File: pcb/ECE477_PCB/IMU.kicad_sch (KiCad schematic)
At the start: 8 parts, among them U5 MPU-9250, U6 LSM6DS3

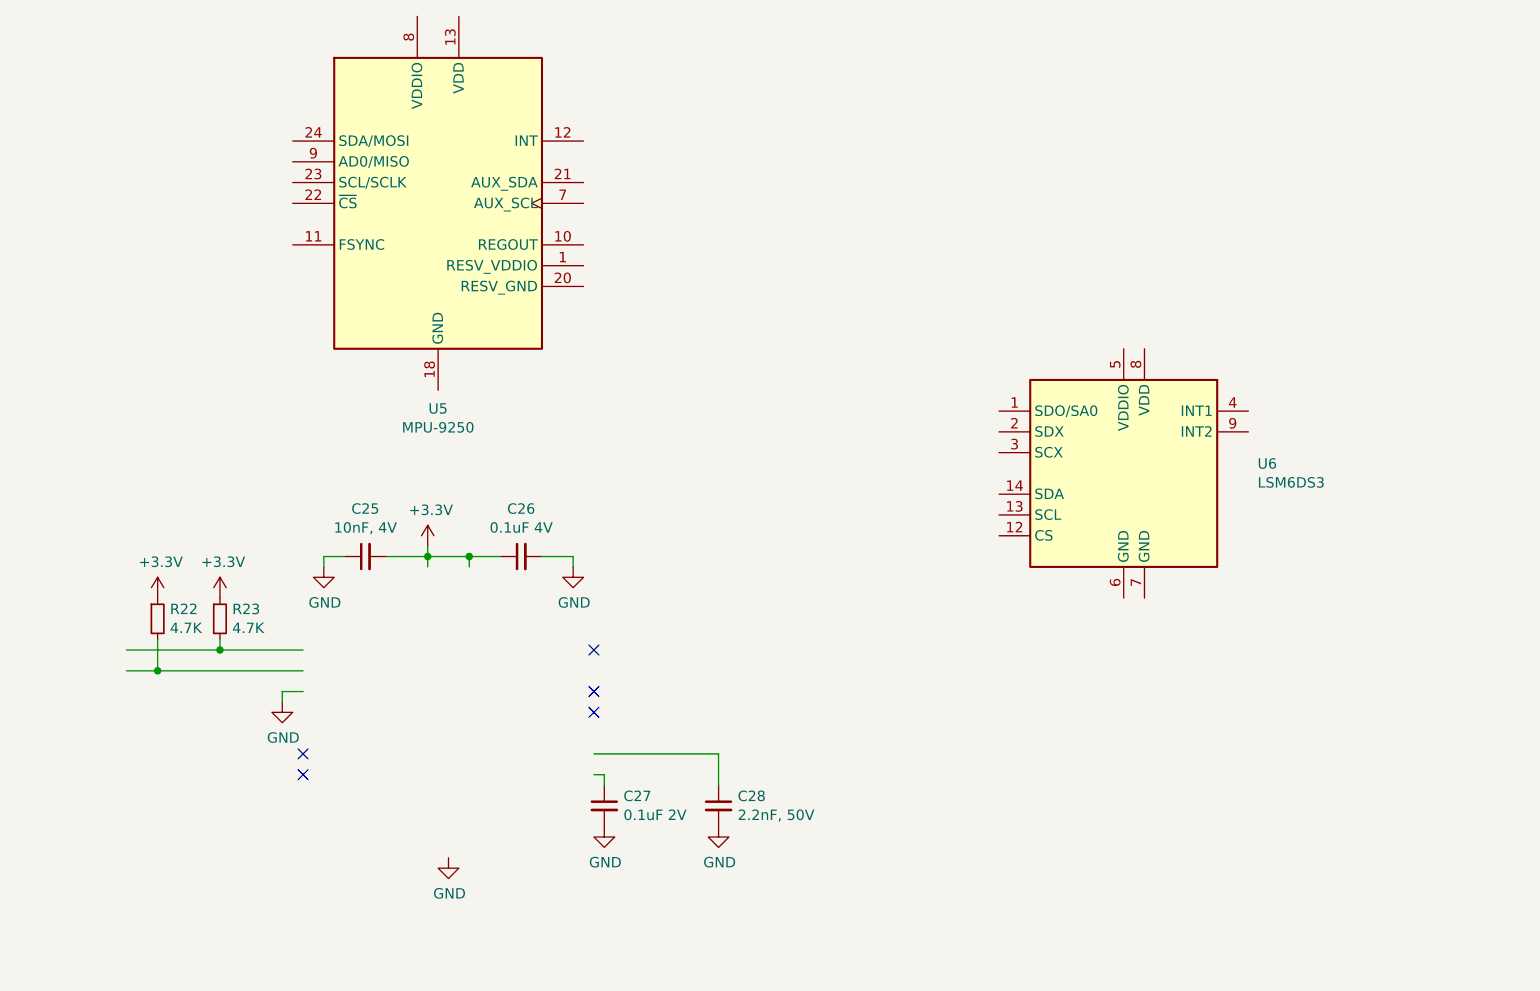
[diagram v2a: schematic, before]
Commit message: completed first rev of PCB. looks like the Pi connector needs moved slightly, board radius is off but drill positions are still the same
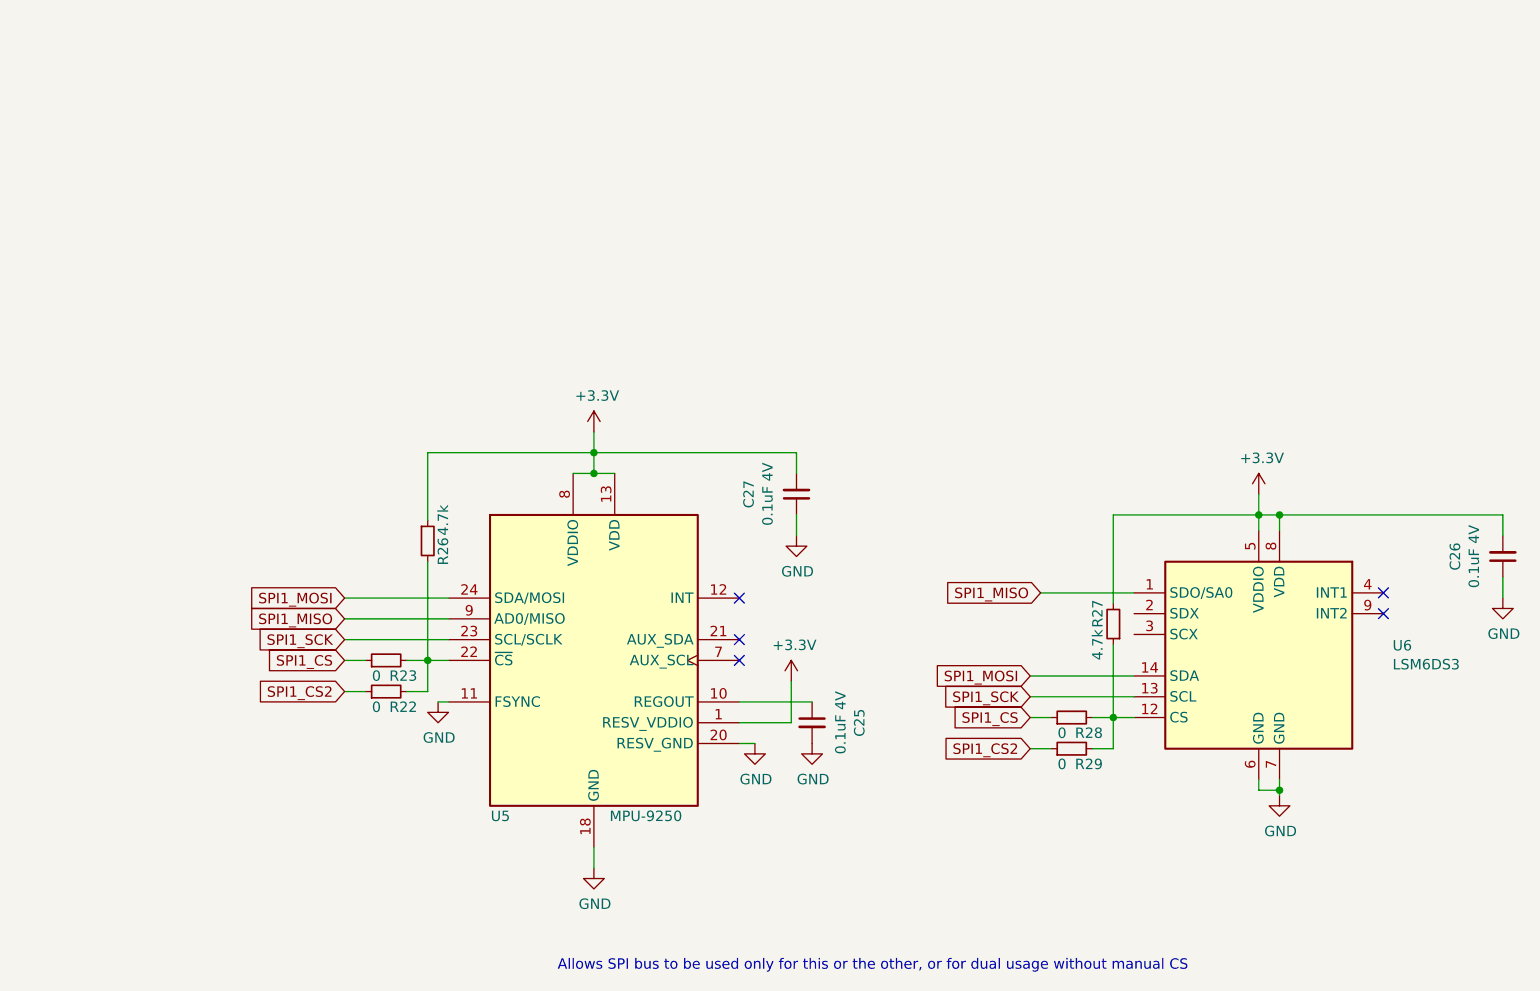
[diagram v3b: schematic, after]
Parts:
- removed C28: 2.2nF, 50V, Capacitor_SMD:C_0603_1608Metric, symbol Device:C_Small
- added R26, R27: 4.7k, Resistor_SMD:R_0603_1608Metric, symbol Device:R_Small
- added R28, R29: 0, Resistor_SMD:R_0603_1608Metric, symbol Device:R_Small
- C25: value 10nF, 4V -> 0.1uF 4V; footprint Capacitor_SMD:C_0402_1005Metric -> Capacitor_SMD:C_0603_1608Metric; LCSC C15195 -> C1525; LCSC Part # C15195 -> C1525
- C26: footprint Capacitor_SMD:C_0402_1005Metric -> Capacitor_SMD:C_0603_1608Metric
- C27: value 0.1uF 2V -> 0.1uF 4V; footprint Capacitor_SMD:C_0402_1005Metric -> Capacitor_SMD:C_0603_1608Metric
- R22, R23: value 4.7K -> 0
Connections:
- net +3V3: now also C26.2, C27.2, U5.1 (RESV_VDDIO), U5.13 (VDD), U5.8 (VDDIO), U6.5 (VDDIO), U6.8 (VDD), R26.1, R27.2; no longer C25.2, C26.1, R22.1, R23.1
- net GND: now also C25.2, C26.1, C27.1, U5.11 (FSYNC), U5.18 (GND), U5.20 (RESV_GND), U6.6 (GND), U6.7 (GND); no longer C25.1, C26.2, C27.2
- net at R22.2: now also R23.2, U5.22 (~{CS}), R26.2
- net at U5.10 (REGOUT): now also C25.1
- net SPI1_SCK: now reaches U5.23 (SCL/SCLK)
- net SPI1_SCK: now also U6.13 (SCL)
- net SPI1_MOSI: now reaches U5.24 (SDA/MOSI)
- net SPI1_MOSI: now also U6.14 (SDA)
- net SPI1_MISO: now reaches U5.9 (AD0/MISO)
- net SPI1_MISO: now also U6.1 (SDO/SA0)
- net at U6.12 (CS): now also R27.1, R28.2, R29.2
- new net SPI1_CS: R23.1, R28.1
- new net SPI1_CS2: R22.1, R29.1
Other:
- note added: "Allows SPI bus to be used only for this or the other, or for dual usage without manual CS"
- moved on the sheet: C26, R22, R23, U5, U6

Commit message: last fixes, ready to order (I think)
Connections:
- net +3V3: now also U6.2 (SDX), U6.3 (SCX)
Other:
- moved on the sheet: R27
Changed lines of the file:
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@@
 (kicad_sch (version 20211123) (generator eeschema)
   (paper "A4")
+  (junction (at 172.72 98.425) (diameter 0) (color 0 0 0 0)
+  )
   (junction (at 110.49 66.04) (diameter 0) (color 0 0 0 0)
   )
@@
   (junction (at 90.17 91.44) (diameter 0) (color 0 0 0 0)
   )
-  (junction (at 173.99 98.425) (diameter 0) (color 0 0 0 0)
-  )
   (junction (at 110.49 68.58) (diameter 0) (color 0 0 0 0)
   )
@@
   (junction (at 191.77 73.66) (diameter 0) (color 0 0 0 0)
   )
+  (junction (at 175.26 73.66) (diameter 0) (color 0 0 0 0)
+  )
+  (junction (at 175.26 85.725) (diameter 0) (color 0 0 0 0)
+  )
+  (no_connect (at 207.01 85.725))
   (no_connect (at 128.27 91.44))
-  (no_connect (at 207.01 83.185))
-  (no_connect (at 207.01 85.725))
   (no_connect (at 128.27 88.9))
   (no_connect (at 128.27 83.82))
+  (no_connect (at 207.01 83.185))
   (wire (pts (xy 90.17 95.25) (xy 90.17 91.44))
     (stroke (width 0) (type default) (color 0 0 0 0))
@@
     (stroke (width 0) (type default) (color 0 0 0 0))
   )
-  (wire (pts (xy 173.99 73.66) (xy 191.77 73.66))
-    (stroke (width 0) (type default) (color 0 0 0 0))
-  )
   (wire (pts (xy 163.83 98.425) (xy 166.37 98.425))
     (stroke (width 0) (type default) (color 0 0 0 0))
   )
-  (wire (pts (xy 171.45 102.235) (xy 173.99 102.235))
+  (wire (pts (xy 171.45 102.235) (xy 172.72 102.235))
     (stroke (width 0) (type default) (color 0 0 0 0))
   )
@@
     (stroke (width 0) (type default) (color 0 0 0 0))
   )
+  (wire (pts (xy 175.26 73.66) (xy 175.26 85.725))
+    (stroke (width 0) (type default) (color 0 0 0 0))
+  )
   (wire (pts (xy 194.31 73.66) (xy 191.77 73.66))
     (stroke (width 0) (type default) (color 0 0 0 0))
   )
+  (wire (pts (xy 172.72 98.425) (xy 176.53 98.425))
+    (stroke (width 0) (type default) (color 0 0 0 0))
+  )
   (wire (pts (xy 191.77 73.66) (xy 191.77 75.565))
     (stroke (width 0) (type default) (color 0 0 0 0))
@@
     (stroke (width 0) (type default) (color 0 0 0 0))
   )
-  (wire (pts (xy 173.99 89.535) (xy 173.99 98.425))
+  (wire (pts (xy 172.72 89.535) (xy 172.72 98.425))
     (stroke (width 0) (type default) (color 0 0 0 0))
   )
@@
     (stroke (width 0) (type default) (color 0 0 0 0))
   )
-  (wire (pts (xy 173.99 98.425) (xy 176.53 98.425))
-    (stroke (width 0) (type default) (color 0 0 0 0))
-  )
   (wire (pts (xy 128.27 99.06) (xy 134.62 99.06))
     (stroke (width 0) (type default) (color 0 0 0 0))
@@
     (stroke (width 0) (type default) (color 0 0 0 0))
   )
+  (wire (pts (xy 175.26 85.725) (xy 175.26 88.265))
+    (stroke (width 0) (type default) (color 0 0 0 0))
+  )
   (wire (pts (xy 80.01 95.25) (xy 82.55 95.25))
     (stroke (width 0) (type default) (color 0 0 0 0))
@@
     (stroke (width 0) (type default) (color 0 0 0 0))
   )
+  (wire (pts (xy 175.26 88.265) (xy 176.53 88.265))
+    (stroke (width 0) (type default) (color 0 0 0 0))
+  )
+  (wire (pts (xy 175.26 73.66) (xy 191.77 73.66))
+    (stroke (width 0) (type default) (color 0 0 0 0))
+  )
   (wire (pts (xy 191.77 71.12) (xy 191.77 73.66))
     (stroke (width 0) (type default) (color 0 0 0 0))
@@
     (stroke (width 0) (type default) (color 0 0 0 0))
   )
+  (wire (pts (xy 194.31 73.66) (xy 221.615 73.66))
+    (stroke (width 0) (type default) (color 0 0 0 0))
+  )
   (wire (pts (xy 194.31 75.565) (xy 194.31 73.66))
     (stroke (width 0) (type default) (color 0 0 0 0))
@@
     (stroke (width 0) (type default) (color 0 0 0 0))
   )
-  (wire (pts (xy 173.99 102.235) (xy 173.99 98.425))
+  (wire (pts (xy 172.72 102.235) (xy 172.72 98.425))
     (stroke (width 0) (type default) (color 0 0 0 0))
   )
@@
     (stroke (width 0) (type default) (color 0 0 0 0))
   )
-  (wire (pts (xy 173.99 84.455) (xy 173.99 73.66))
+  (wire (pts (xy 172.72 84.455) (xy 172.72 73.66))
     (stroke (width 0) (type default) (color 0 0 0 0))
   )
@@
     (stroke (width 0) (type default) (color 0 0 0 0))
   )
-  (wire (pts (xy 171.45 98.425) (xy 173.99 98.425))
-    (stroke (width 0) (type default) (color 0 0 0 0))
-  )
-  (wire (pts (xy 221.615 73.66) (xy 194.31 73.66))
+  (wire (pts (xy 172.72 73.66) (xy 175.26 73.66))
+    (stroke (width 0) (type default) (color 0 0 0 0))
+  )
+  (wire (pts (xy 171.45 98.425) (xy 172.72 98.425))
     (stroke (width 0) (type default) (color 0 0 0 0))
   )
@@
   )
   (wire (pts (xy 110.49 66.04) (xy 110.49 68.58))
+    (stroke (width 0) (type default) (color 0 0 0 0))
+  )
+  (wire (pts (xy 175.26 85.725) (xy 176.53 85.725))
     (stroke (width 0) (type default) (color 0 0 0 0))
   )
@@
     (pin "1")
   )
-  (symbol (lib_id "Device:R_Small") (at 173.99 86.995 180) (unit 1)
-    (in_bom yes) (on_board yes)
-    (property "Reference" "R27" (id 0) (at 172.085 85.725 90))
-    (property "Value" "4.7k" (id 1) (at 172.085 89.535 90))
-    (property "Footprint" "Resistor_SMD:R_0603_1608Metric" (id 2) (at 173.99 86.995 0)
-      (effects (font (size 1.27 1.27)) hide)
-    )
-    (property "Datasheet" "~" (id 3) (at 173.99 86.995 0)
-      (effects (font (size 1.27 1.27)) hide)
-    )
+  (symbol (lib_id "Device:R_Small") (at 172.72 86.995 180) (unit 1)
+    (in_bom yes) (on_board yes)
+    (property "Reference" "R27" (id 0) (at 170.815 85.725 90))
+    (property "Value" "4.7k" (id 1) (at 170.815 89.535 90))
+    (property "Footprint" "Resistor_SMD:R_0603_1608Metric" (id 2) (at 172.72 86.995 0)
+      (effects (font (size 1.27 1.27)) hide)
+    )
+    (property "Datasheet" "~" (id 3) (at 172.72 86.995 0)
+      (effects (font (size 1.27 1.27)) hide)
+    )
